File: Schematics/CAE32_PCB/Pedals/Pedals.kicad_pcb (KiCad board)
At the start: 4 copper layers, 86 x 62 mm, 127 parts, among them J1 Conn_01x19_Pin, J10 Conn_01x03_Female, J11 Conn_01x03_Female, J13 Conn_01x03_Female, J14 Conn_01x03_Female, J15 USB_C_Receptacle_USB2.0, J17 LC, J18 LC, J19 LC, J5 Conn_01x03_Female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

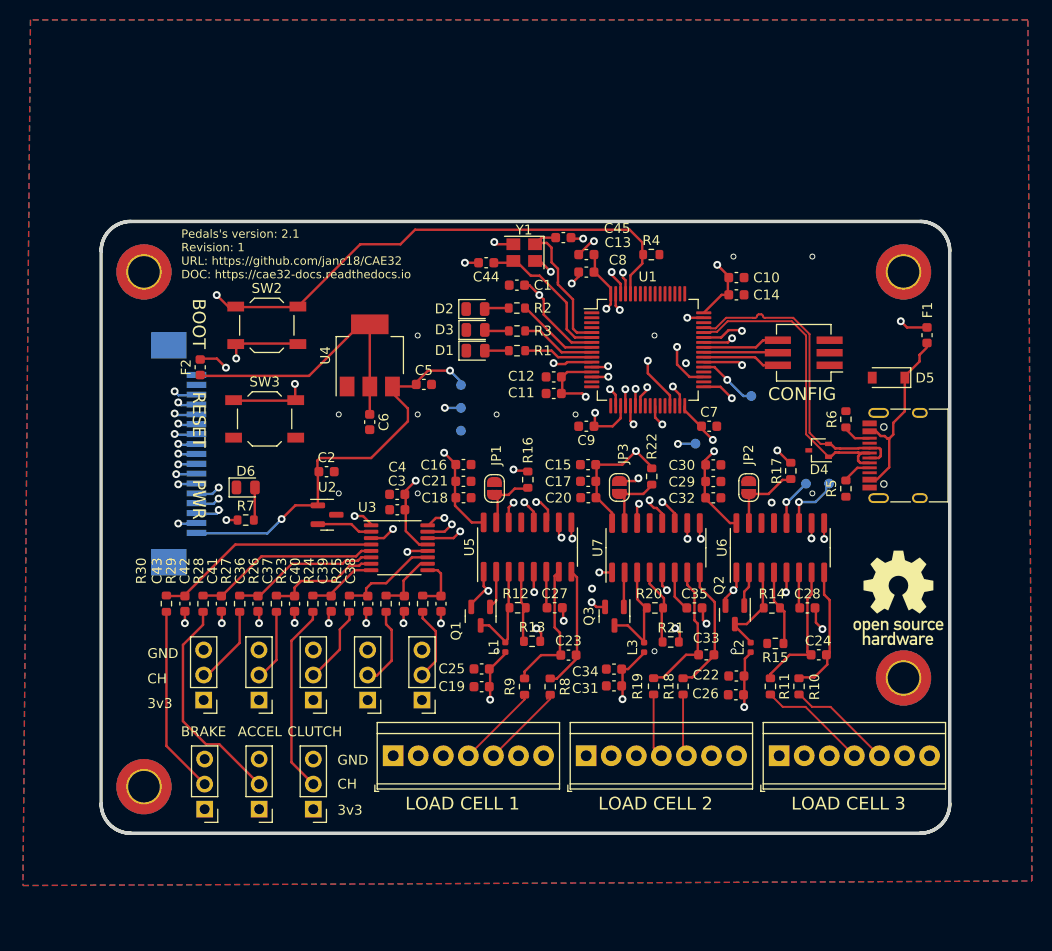
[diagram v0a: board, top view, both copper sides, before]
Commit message: updated: Pcb design, fixed plane grounds and minor improvements, added stlink connector, updated BOM with the current market stock
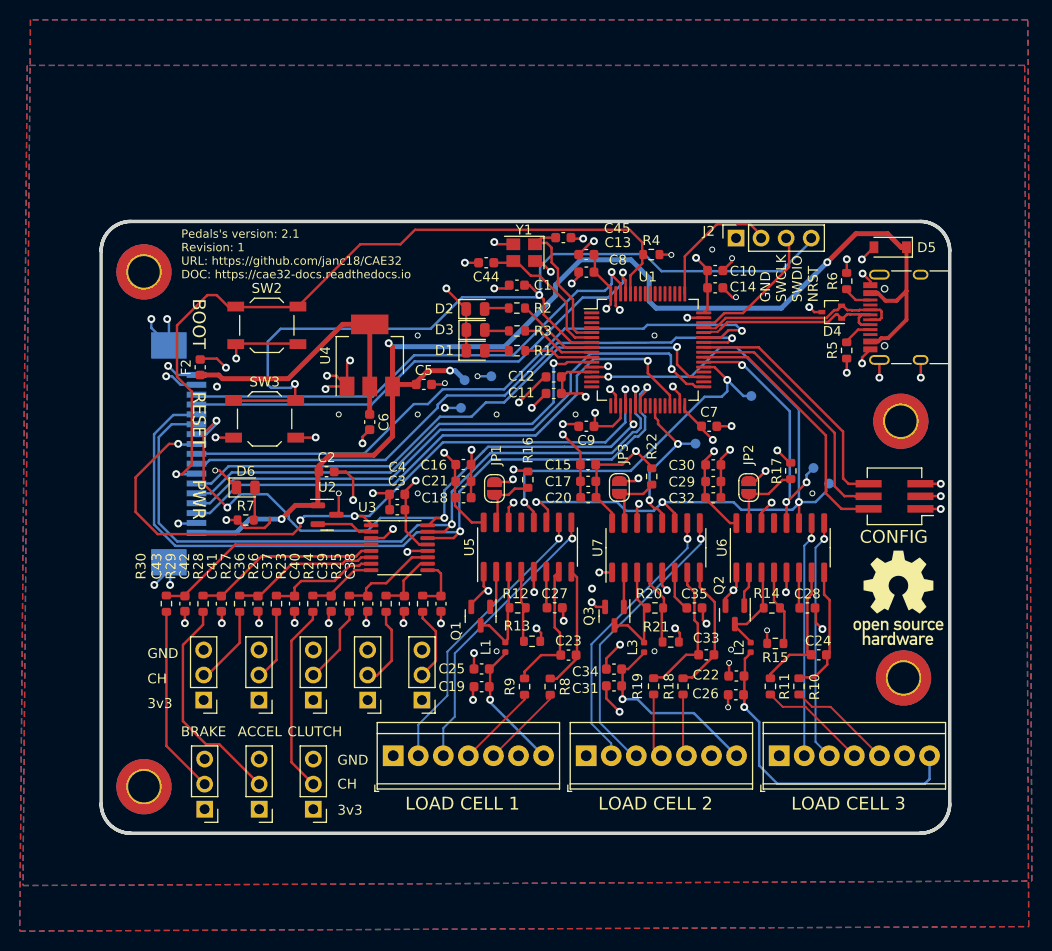
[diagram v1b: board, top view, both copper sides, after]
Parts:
- removed F1: 0467002-NRHF, Fuse:Fuse_0603_1608Metric
- added J2: ST-LINK, Connector_PinSocket_2.54mm:PinSocket_1x04_P2.54mm_Vertical, F.Cu at (162.2, 75.0)
- R16, R17, R22: value 10k -> 10K
- U3: value ADC128S022 -> ADC128S102
- Y1: value Crystal_GND24_Small -> 8 MHz
- moved SW1 17.2 mm to (178.3, 101.2)
- moved H4 15.1 mm to (178.9, 93.6)
- moved D4 14.1 mm to (171.9, 82.5)
- moved J15 14.0 mm to (179.9, 83.1)
- moved R5 14.0 mm to (173.5, 86.4)
- moved R6 14.0 mm to (173.5, 79.4)
- moved D5 13.2 mm to (177.9, 76.0)
- moved TP1 6.32 mm to (137.4, 89.0)
- moved C10 2.26 mm to (160.1, 78.3)
- moved C14 2.26 mm to (160.1, 80.1)
- moved TP5 1.76 mm to (170.1, 98.3)
- moved TP2 0.62 mm to (134.8, 89.5)
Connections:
- D5 pad 1: Net-(D5-A1) -> +5V
- J15 pad A4: Net-(D5-A1) -> +5V
- J15 pad A9: Net-(D5-A1) -> +5V
- J15 pad B4: Net-(D5-A1) -> +5V
- J15 pad B9: Net-(D5-A1) -> +5V
- U1 pad 46: unconnected-(U1-PA13-Pad46) -> /SWDIO
- U1 pad 49: unconnected-(U1-PA14-Pad49) -> /SWCLK
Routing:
- net GNDREF: track 54.9 -> 180.9 mm, vias 48 -> 96
- net +5V: track 92.6 -> 126.3 mm, vias 3 -> 4
- net /NRST: track 54.8 -> 88.1 mm
- net /B2: track 6.79 -> 25.9 mm
- net /B3: track 7.85 -> 26.5 mm
- net /B1: track 7.81 -> 25.2 mm
- net Net-(D5-A1): track 17.0 -> 0.00 mm
- net /SWDIO: track 0.00 -> 13.9 mm
- net /SWCLK: track 0.00 -> 13.8 mm
- net /CS_ADC: track 61.4 -> 73.8 mm, vias 3 -> 4
- net /D-: track 31.9 -> 21.1 mm
- net /D+: track 31.8 -> 21.2 mm
- net Net-(J17-Pin_7): track 26.6 -> 32.9 mm
- net /Load Cells/B2+: track 35.6 -> 29.6 mm
- net /S_CS_PEDALS: track 66.9 -> 61.0 mm, vias 3 -> 1
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- added copper zone on B.Cu, net +3.3V
- added copper zone on F.Cu, net +3.3V
- added copper zone on In1.Cu, net GNDREF
- added copper zone on In2.Cu, net GNDREF
- removed copper zone on In1.Cu, net +3.3V
- removed copper zone on In2.Cu, net +3.3V
- removed copper zone on B.Cu, net GNDREF
- removed copper zone on F.Cu, net GNDREF
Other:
- board text added: "GND SWCLK SWDIO NRST"

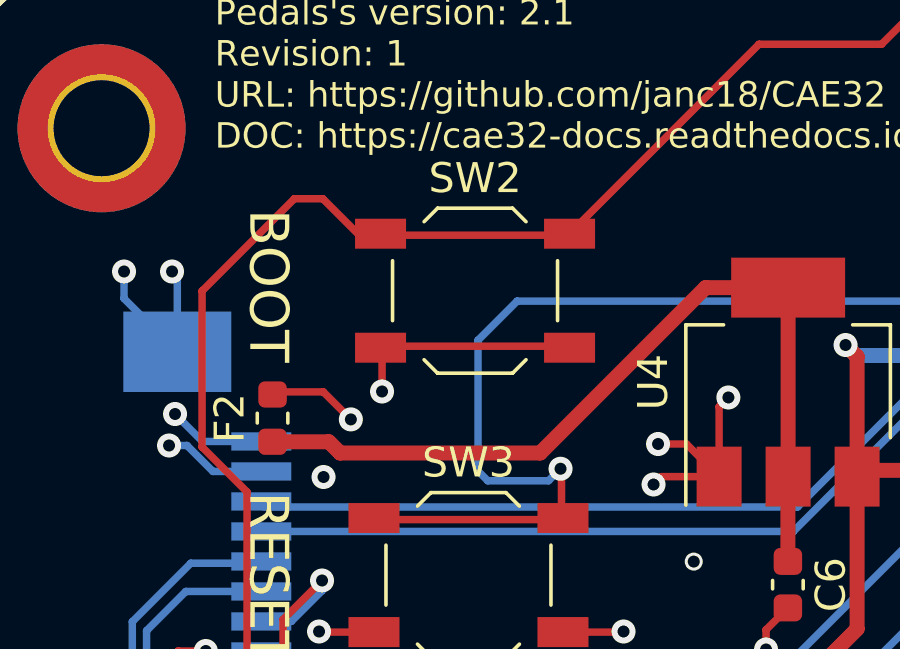
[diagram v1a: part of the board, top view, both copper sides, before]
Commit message: fixed: changed fuse footprint for the correct one(0805)
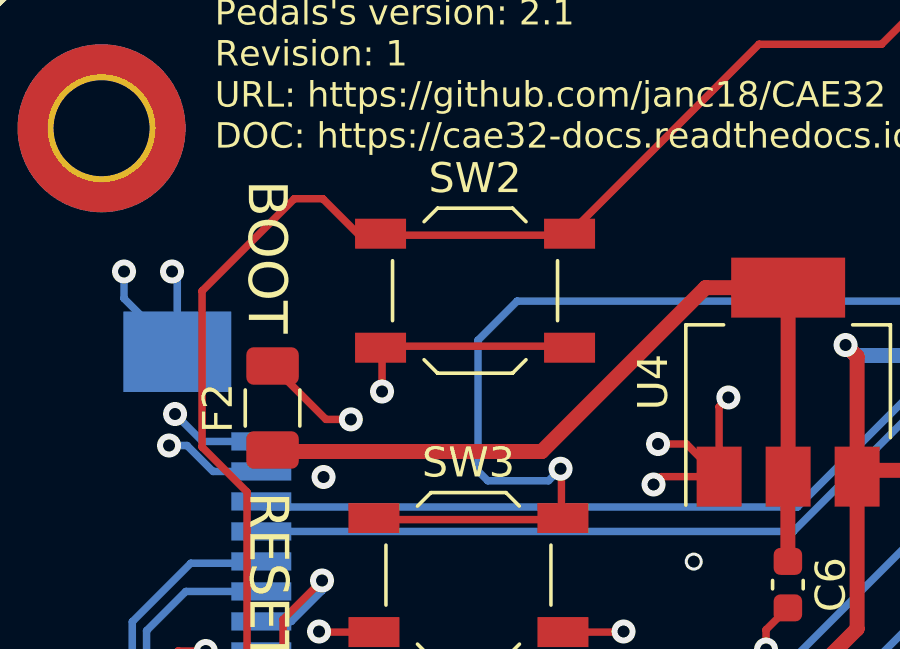
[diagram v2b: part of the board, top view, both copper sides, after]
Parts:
- F2: footprint Fuse:Fuse_0603_1608Metric -> Fuse:Fuse_1206_3216Metric
- moved F2 0.34 mm to (108.0, 87.8)
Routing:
- net Net-(U4-VO): track 28.8 -> 28.3 mm

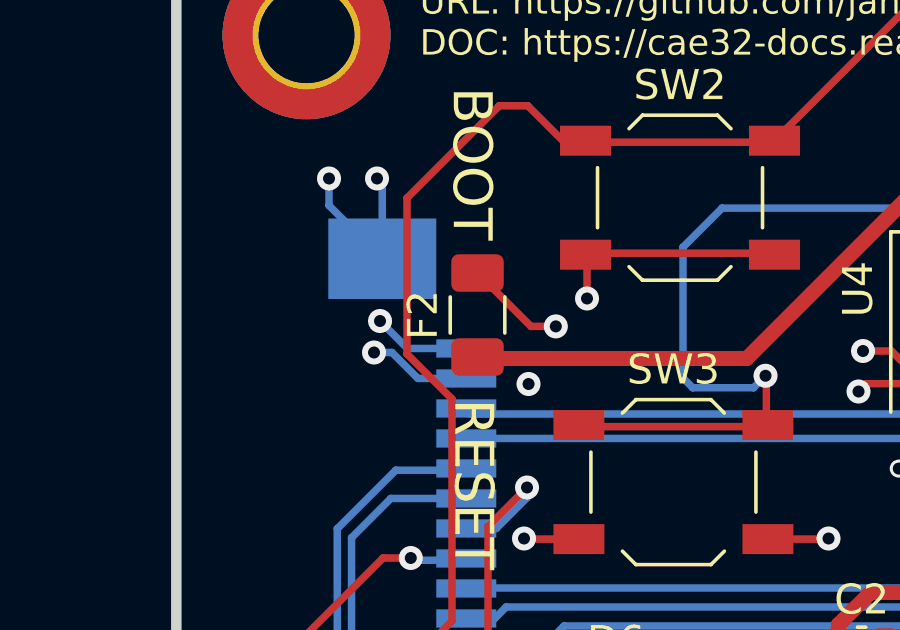
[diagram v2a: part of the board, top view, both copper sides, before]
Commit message: fixed: changed fuse footprint to 1206
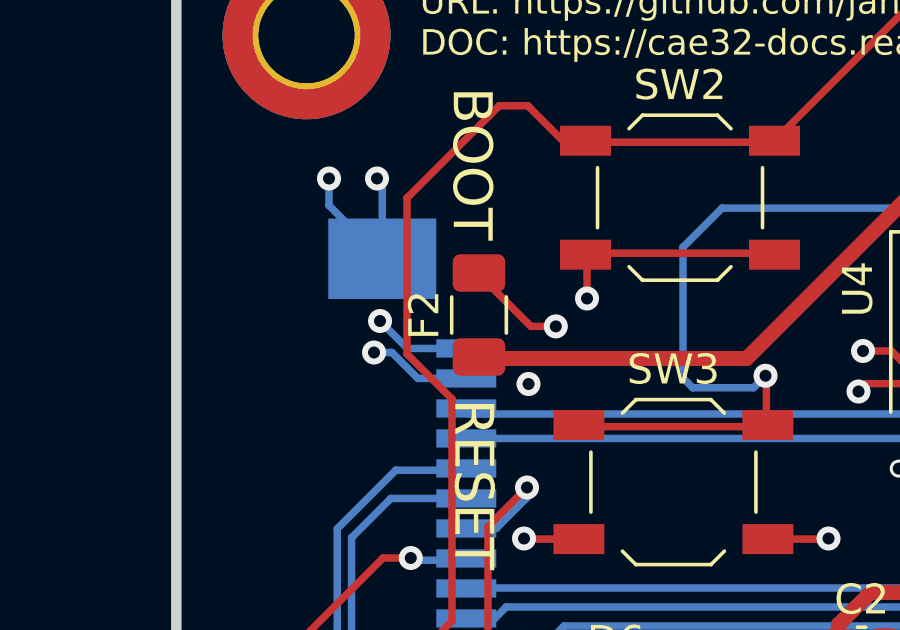
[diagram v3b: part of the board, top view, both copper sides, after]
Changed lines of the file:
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@@
 	(footprint "Fuse:Fuse_1206_3216Metric"
 		(layer "F.Cu")
-		(at 107.95 87.8 90)
+		(at 108 87.8 90)
 		(descr "Fuse SMD 1206 (3216 Metric), square (rectangular) end terminal, IPC_7351 nominal, (Body size source: http://www.tortai-tech.com/upload/download/2011102023233369053.pdf), generated with kicad-footprint-generator")
 		(tags "fuse")

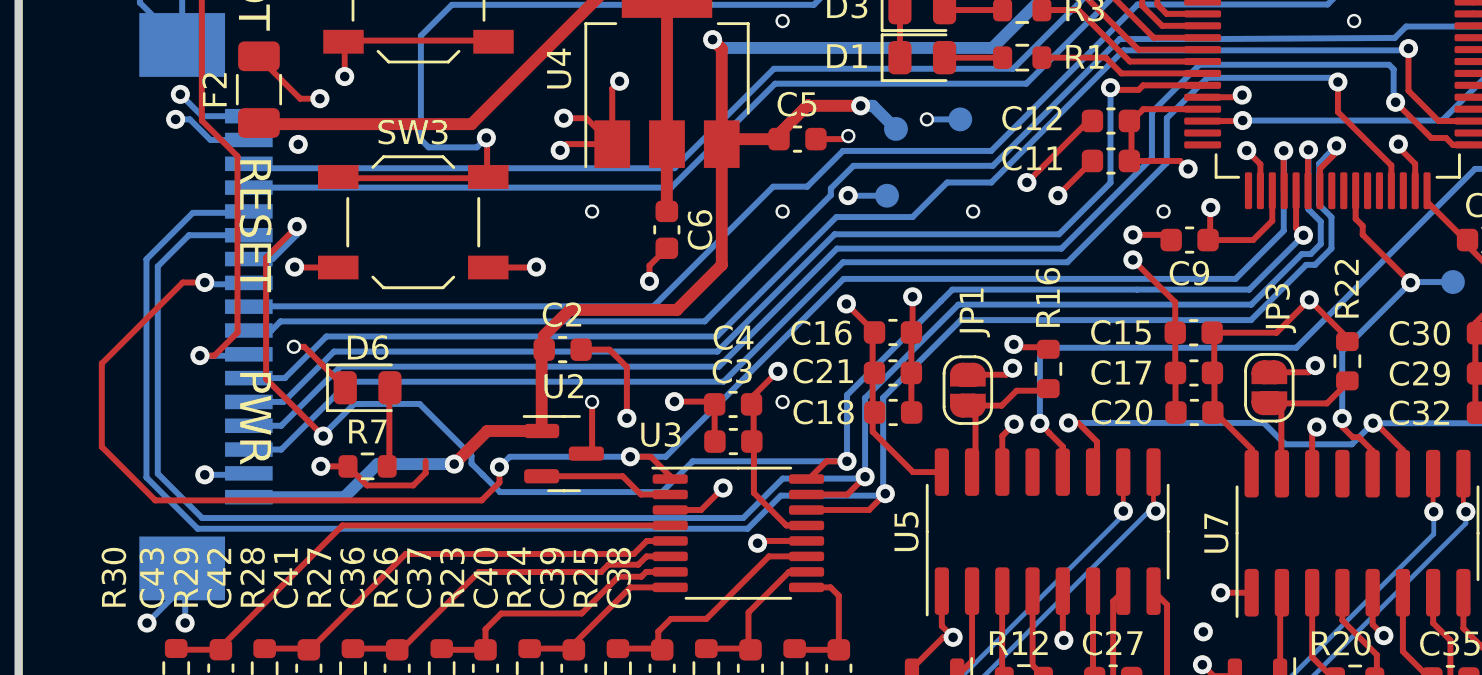
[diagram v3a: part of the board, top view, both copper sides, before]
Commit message: fixed: SPI route
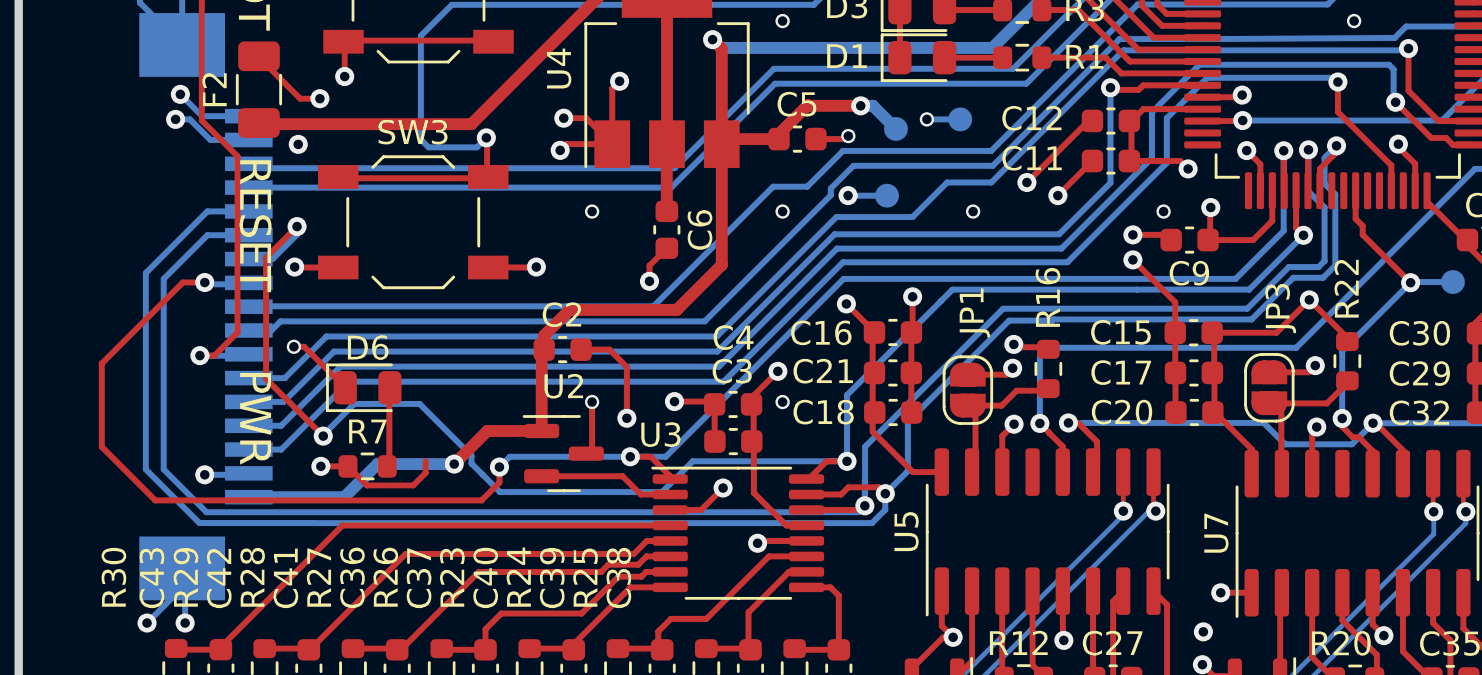
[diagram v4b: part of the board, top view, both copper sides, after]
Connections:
- J1 pad 12: /DOUT -> /MISO
- J1 pad 13: /DIN -> /MOSI
- U1 pad 22: /DOUT -> /MISO
- U1 pad 23: /DIN -> /MOSI
- U2 pad 2: Net-(U2-OUT) -> unconnected-(U2-OUT-Pad2)
- U3 pad 14: /DIN -> /MISO
- U3 pad 15: /DOUT -> /MOSI
- U3 pad 2: Net-(U2-OUT) -> unconnected-(U3-VA-Pad2)
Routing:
- net /DIN: track 82.9 -> 0.00 mm, vias 2 -> 0
- net /MOSI: track 0.00 -> 82.0 mm, vias 0 -> 2
- net /DOUT: track 78.3 -> 0.00 mm, vias 2 -> 0
- net /MISO: track 0.00 -> 78.1 mm, vias 0 -> 2
- net Net-(U2-OUT): track 5.72 -> 0.00 mm
- net (no net): track 0.00 -> 5.72 mm

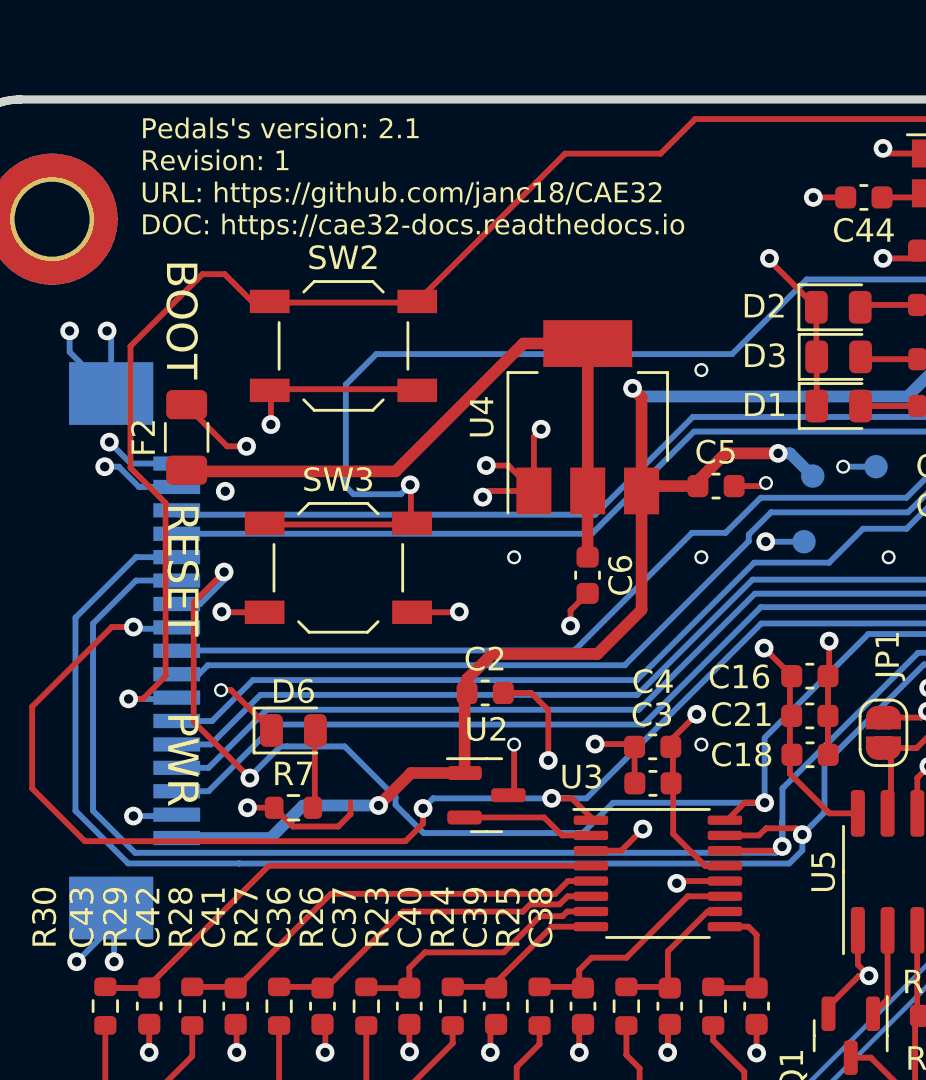
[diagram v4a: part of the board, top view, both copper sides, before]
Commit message: fixed: SPI route and updated kicad versions in schematic and pcb design
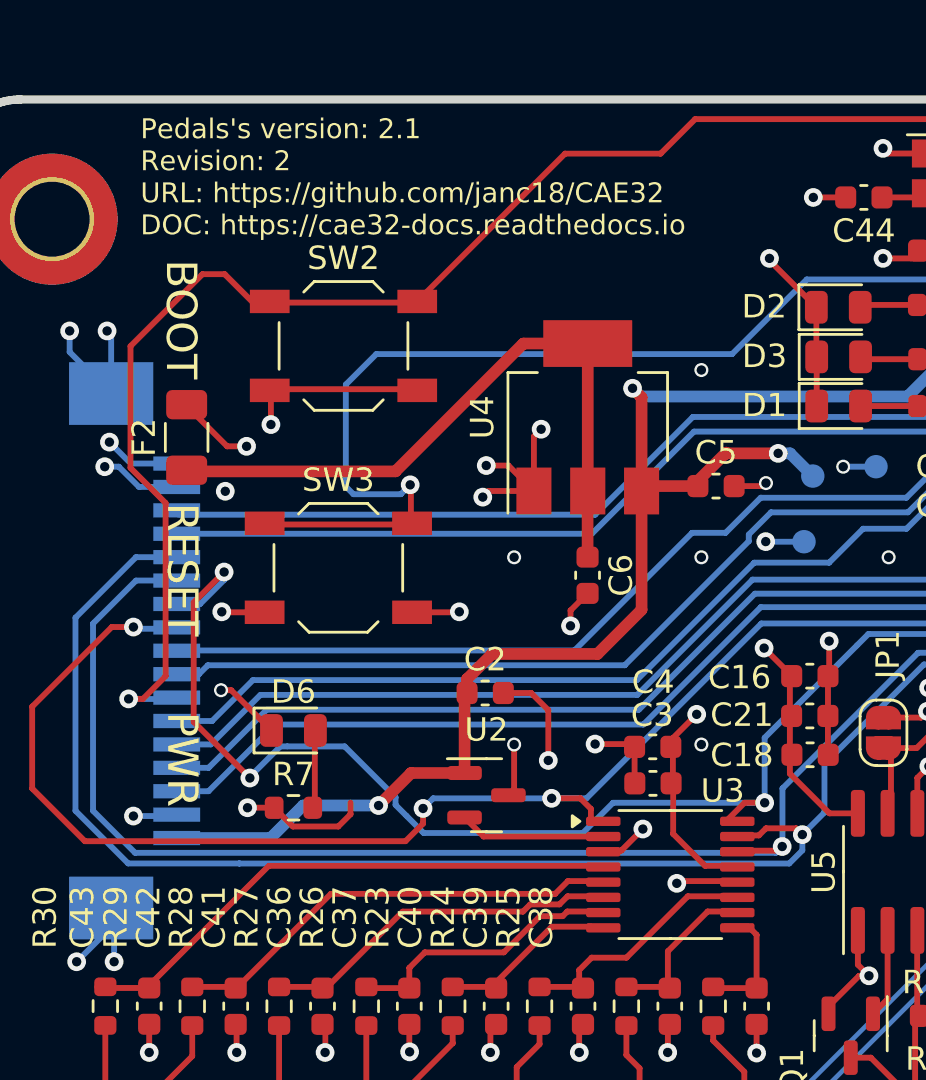
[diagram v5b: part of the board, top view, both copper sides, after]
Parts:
- moved U3 0.53 mm to (128.7, 106.5)
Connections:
- U2 pad 2: unconnected-(U2-OUT-Pad2) -> Net-(U2-OUT)
- U3 pad 2: unconnected-(U3-VA-Pad2) -> Net-(U2-OUT)
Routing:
- net Net-(U2-OUT): track 0.00 -> 6.26 mm
- net (no net): track 5.72 -> 0.00 mm
- net /MISO: track 78.1 -> 77.1 mm
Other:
- board text added: "Pedals's version: 2.1 Revision: 2 URL: https://github.com/janc18/CAE32 DOC: https://cae32-docs.readthedocs.io"
- board text removed: "Pedals's version: 2.1 Revision: 1 URL: https://github.com/janc18/CAE32 DOC: https://cae32-docs.readthedocs.io"
